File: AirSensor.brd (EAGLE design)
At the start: 108.6 x 80 mm, 32 parts, among them J1 battery Output 7.4V, J2 10118194-0001LF, U1 ATSAMD21G18A-AU, Y1 32.768kHz

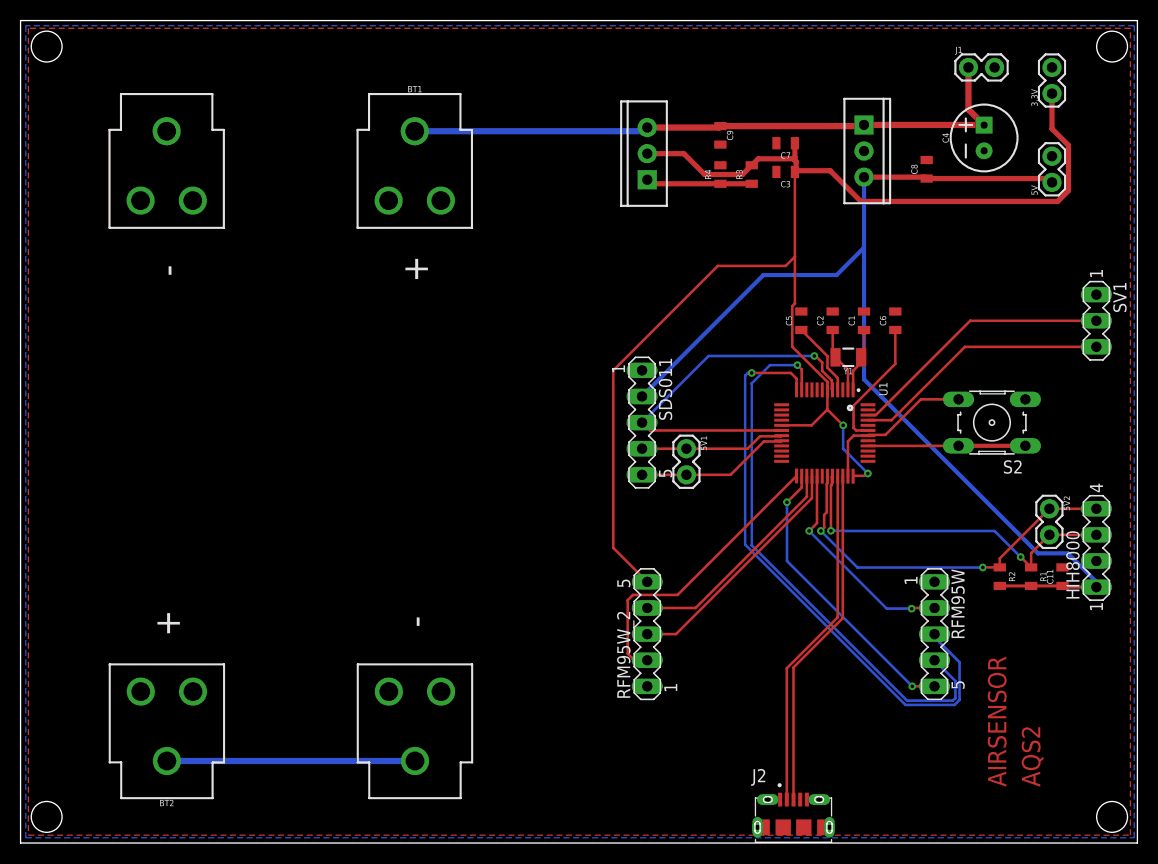
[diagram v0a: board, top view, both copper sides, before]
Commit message: added JTAG schematic and PCB  + all pictures
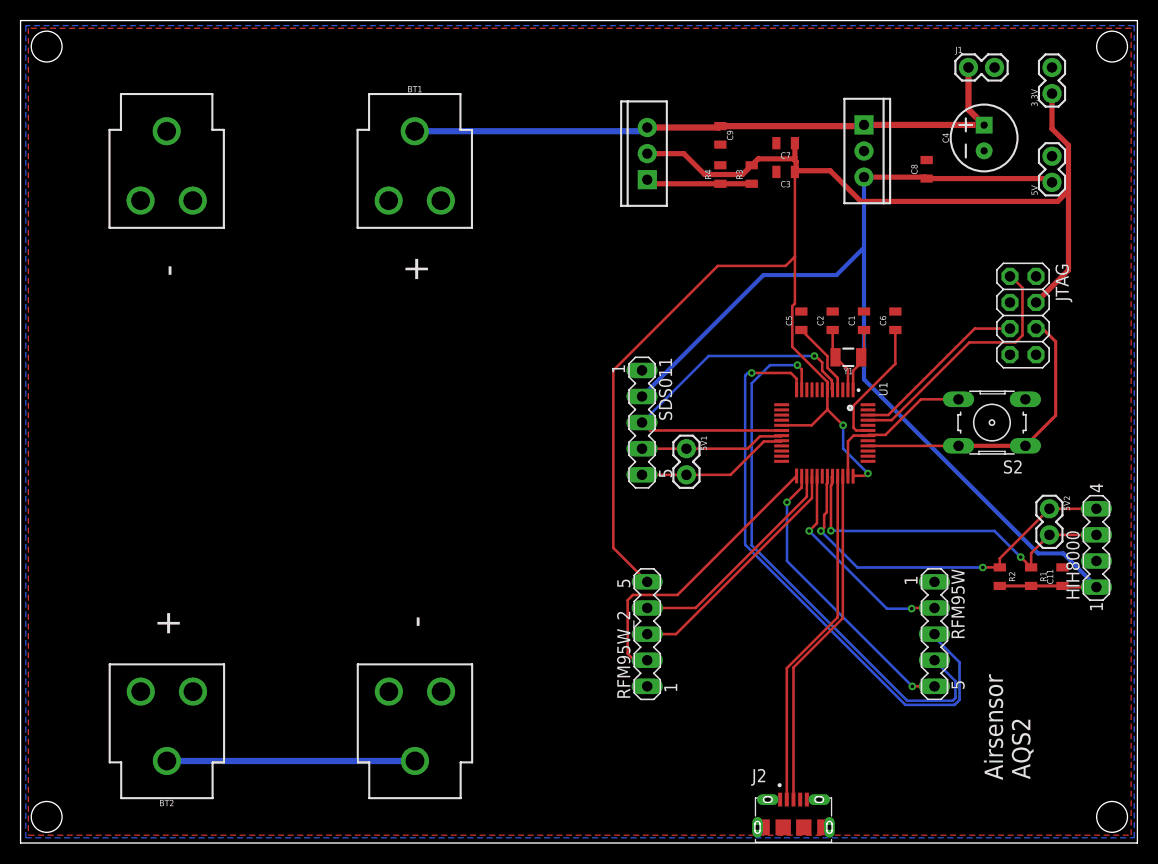
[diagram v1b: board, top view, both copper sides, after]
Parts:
- removed SV1: (no value), con-lstb:MA03-1
- added JTAG: (no value), adafruit:2X04
- HIH8000: value Temp and humid sensor -> T and H sensor
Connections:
- net 3.3V: now also JTAG.4
- net GND: now also JTAG.2
- net N$10: now also JTAG.6
- net N$15: now also JTAG.1; no longer SV1.3
- net N$16: now also JTAG.5; no longer SV1.2
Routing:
- net N$10: track 15.3 -> 29.1 mm
- net 3.3V: track 140.3 -> 152.5 mm
- net N$16: track 26.0 -> 17.3 mm
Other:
- board text added: "Airsensor"
- board text removed: "AIRSENSOR"
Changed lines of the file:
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@@
 <setting verticaltext="up"/>
 </settings>
-<grid distance="5" unitdist="mil" unit="mil" style="dots" multiple="1" display="yes" altdistance="5" altunitdist="mil" altunit="mil"/>
+<grid distance="1" unitdist="mil" unit="mil" style="dots" multiple="1" display="yes" altdistance="5" altunitdist="mil" altunit="mil"/>
 <layers>
 <layer number="1" name="Top" color="4" fill="1" visible="yes" active="yes"/>
@@
 </layers>
 <board>
+<fusionsync huburn="a.YnVzaW5lc3M6c2t5bmV0MTMz" projecturn="a.YnVzaW5lc3M6c2t5bmV0MTMzI0QyMDE5MTAzMTIzMzQxNDY3Ng" f3durn="urn:adsk.wipprod:dm.lineage:1Ub-EbivQau2BrcJynC3oQ" pcbguid="" lastpulledtime="" lastsyncedchangeguid="" latestrevisionid="78f90f56-6bf9-44d5-9f1f-b04a8c04fa7a" lastsyncedrevisionid="78f90f56-6bf9-44d5-9f1f-b04a8c04fa7a" lastboardhashguid="26696e0e-a0db-138f-774c-2213d21c3754" lastpushedtime="2020-10-21T16:27:33Z" linktopcb3d="true"/>
 <plain>
 <wire x1="0" y1="0" x2="108.636" y2="0" width="0" layer="20"/>
@@
 <wire x1="108.636" y1="80" x2="0" y2="80" width="0" layer="20"/>
 <wire x1="0" y1="80" x2="0" y2="0" width="0" layer="20"/>
-<dimension x1="60.96" y1="25.4" x2="88.9" y2="25.4" x3="74.93" y3="28.448" textsize="1.778" layer="1"/>
-<dimension x1="60.96" y1="0.254" x2="60.96" y2="25.4" x3="52.324" y3="12.827" textsize="1.778" layer="1"/>
 <hole x="2.54" y="2.54" drill="3"/>
 <hole x="2.54" y="77.47" drill="3"/>
 <hole x="106.172" y="77.47" drill="3"/>
 <hole x="106.172" y="2.54" drill="3"/>
-<text x="95.885" y="5.461" size="1.778" layer="1" rot="R90">AIRSENSOR</text>
-<text x="99.187" y="5.461" size="1.778" layer="1" rot="R90">AQS2</text>
+<dimension x1="0" y1="0" x2="108.636" y2="0" x3="54.318" y3="-3.7084" textsize="1.778" layer="1"/>
+<dimension x1="0" y1="0" x2="0" y2="80" x3="-2.1336" y3="40" textsize="1.778" layer="1"/>
+<text x="95.5548" y="6.1214" size="1.778" layer="25" rot="R90">Airsensor</text>
+<text x="98.2218" y="6.1976" size="1.778" layer="25" rot="R90">AQS2</text>
 </plain>
 <attributes>
@@
 <attribute name="VALUE" x="57.531" y="43.434" size="1.27" layer="27" ratio="10" rot="R270"/>
 </element>
-<element name="HIH8000" library="con-lstb" library_urn="urn:adsk.eagle:library:162" package="MA04-1" package3d_urn="urn:adsk.eagle:package:8337/1" value="Temp and humid sensor" x="104.648" y="28.702" smashed="yes" rot="R90">
+<element name="HIH8000" library="con-lstb" library_urn="urn:adsk.eagle:library:162" package="MA04-1" package3d_urn="urn:adsk.eagle:package:8337/1" value="T and H sensor" x="104.648" y="28.702" smashed="yes" rot="R90">
 <attribute name="MF" value="" x="104.648" y="28.702" size="1.778" layer="27" rot="R90" display="off"/>
 <attribute name="MPN" value="" x="104.648" y="28.702" size="1.778" layer="27" rot="R90" display="off"/>
@@
 <attribute name="OC_NEWARK" value="unknown" x="104.648" y="28.702" size="1.778" layer="27" rot="R90" display="off"/>
 <attribute name="POPULARITY" value="41" x="104.648" y="28.702" size="1.778" layer="27" rot="R90" display="off"/>
-<attribute name="VALUE" x="102.997" y="29.337" size="1.27" layer="27" ratio="10" rot="R90"/>
-</element>
-<element name="SV1" library="con-lstb" library_urn="urn:adsk.eagle:library:162" package="MA03-1" package3d_urn="urn:adsk.eagle:package:8339/1" value="" x="104.648" y="50.8" smashed="yes" rot="R270">
-<attribute name="MF" value="" x="104.648" y="50.8" size="1.778" layer="27" rot="R270" display="off"/>
-<attribute name="MPN" value="" x="104.648" y="50.8" size="1.778" layer="27" rot="R270" display="off"/>
-<attribute name="NAME" x="106.299" y="54.61" size="1.27" layer="25" ratio="10" rot="R270"/>
-<attribute name="OC_FARNELL" value="unknown" x="104.648" y="50.8" size="1.778" layer="27" rot="R270" display="off"/>
-<attribute name="OC_NEWARK" value="unknown" x="104.648" y="50.8" size="1.778" layer="27" rot="R270" display="off"/>
-<attribute name="POPULARITY" value="48" x="104.648" y="50.8" size="1.778" layer="27" rot="R270" display="off"/>
-<attribute name="VALUE" x="101.727" y="54.61" size="1.27" layer="27" ratio="10" rot="R270"/>
+<attribute name="VALUE" x="107.5182" y="22.5806" size="1.27" layer="27" ratio="10" rot="R90"/>
 </element>
 <element name="RFM95W" library="con-lstb" library_urn="urn:adsk.eagle:library:162" package="MA05-1" package3d_urn="urn:adsk.eagle:package:8332/1" value="LoRa1" x="88.9" y="20.32" smashed="yes" rot="R270">
@@
 <attribute name="PROD_ID" value="CAP-08064" x="101.346" y="25.908" size="1.778" layer="27" rot="R90" display="off"/>
 <attribute name="VALUE" x="102.235" y="25.908" size="0.6096" layer="27" font="vector" ratio="20" rot="R90" align="top-center"/>
+</element>
+<element name="JTAG" library="adafruit" library_urn="urn:adsk.eagle:library:420" package="2X04" package3d_urn="urn:adsk.eagle:package:6240893/1" value="" x="97.5106" y="51.308" smashed="yes" rot="R270">
+<attribute name="NAME" x="100.6856" y="56.388" size="1.27" layer="25" ratio="10" rot="R270"/>
+<attribute name="VALUE" x="93.0656" y="56.388" size="1.27" layer="27" rot="R270"/>
 </element>
 </elements>
@@
 <vertex x="0.762" y="79.248"/>
 <vertex x="0.762" y="0.762"/>
-<vertex x="107.95" y="0.762"/>
-<vertex x="107.95" y="79.248"/>
+<vertex x="108.0262" y="0.762"/>
+<vertex x="108.0262" y="79.248"/>
 </polygon>
 <polygon width="0.1524" layer="16" isolate="0.508">
@@
 <wire x1="81.03" y1="39.628" x2="82.432" y2="39.628" width="0.254" layer="1"/>
 <wire x1="80.482" y1="39.08" x2="81.03" y2="39.628" width="0.254" layer="1"/>
+<contactref element="JTAG" pad="2"/>
 <wire x1="73.522" y1="68.072" x2="73.522" y2="65.278" width="0" layer="19" extent="1-1"/>
 </signal>
@@
 <wire x1="91.2368" y1="38.6334" x2="87.8278" y2="38.628" width="0.254" layer="1"/>
 <wire x1="87.8278" y1="38.628" x2="82.432" y2="38.628" width="0.254" layer="1"/>
+<contactref element="JTAG" pad="6"/>
+<wire x1="97.7392" y1="38.6334" x2="100.6856" y2="41.5798" width="0.3048" layer="1"/>
+<wire x1="100.6856" y1="41.5798" x2="100.6856" y2="48.768" width="0.3048" layer="1"/>
+<wire x1="100.6856" y1="48.768" x2="99.4156" y2="50.038" width="0.3048" layer="1"/>
+<wire x1="99.4156" y1="50.038" x2="98.7806" y2="50.038" width="0.3048" layer="1"/>
 </signal>
 <signal name="N$11">
@@
 <wire x1="79.375" y1="55.245" x2="82.042" y2="57.912" width="0.4064" layer="16"/>
 <wire x1="82.042" y1="57.912" x2="82.042" y2="64.77" width="0.4064" layer="16"/>
-<wire x1="104.648" y1="24.892" x2="104.648" y2="25.4" width="0.4064" layer="16"/>
-<wire x1="104.648" y1="25.4" x2="101.8794" y2="28.1686" width="0.4064" layer="16"/>
-<wire x1="101.8794" y1="28.1686" x2="98.97806875" y2="28.1686" width="0.4064" layer="16"/>
+<wire x1="104.648" y1="24.892" x2="104.648" y2="24.9428" width="0.4064" layer="16"/>
+<wire x1="104.648" y1="24.9428" x2="101.4222" y2="28.1686" width="0.4064" layer="16"/>
+<wire x1="101.4222" y1="28.1686" x2="98.97806875" y2="28.1686" width="0.4064" layer="16"/>
 <wire x1="98.97806875" y1="28.1686" x2="82.042" y2="45.10466875" width="0.4064" layer="16"/>
 <wire x1="82.042" y1="45.10466875" x2="82.042" y2="57.912" width="0.4064" layer="16"/>
@@
 <wire x1="82.423" y1="35.941" x2="82.204" y2="35.722" width="0.254" layer="1"/>
 <wire x1="82.204" y1="35.722" x2="81.026" y2="35.722" width="0.254" layer="1"/>
+<contactref element="JTAG" pad="4"/>
+<wire x1="98.7806" y1="52.578" x2="101.9302" y2="55.7276" width="0.508" layer="1"/>
+<wire x1="101.9302" y1="55.7276" x2="101.9302" y2="63.45038125" width="0.508" layer="1"/>
 <wire x1="80.01" y1="40.628" x2="82.432" y2="40.628" width="0" layer="19" extent="1-1"/>
 </signal>
@@
 </signal>
 <signal name="N$15">
-<contactref element="SV1" pad="3"/>
 <contactref element="U1" pad="45"/>
-<wire x1="104.648" y1="48.26" x2="91.85813125" y2="48.26" width="0.254" layer="1"/>
-<wire x1="84.72613125" y1="41.128" x2="82.432" y2="41.128" width="0.254" layer="1"/>
-<wire x1="91.85813125" y1="48.26" x2="84.72613125" y2="41.128" width="0.254" layer="1"/>
+<wire x1="82.432" y1="41.128" x2="84.72613125" y2="41.128" width="0.254" layer="1"/>
+<contactref element="JTAG" pad="1"/>
+<wire x1="92.28993125" y1="48.6918" x2="96.774" y2="48.6918" width="0.254" layer="1"/>
+<wire x1="96.774" y1="48.6918" x2="97.4598" y2="49.3776" width="0.254" layer="1"/>
+<wire x1="97.4598" y1="49.3776" x2="97.4598" y2="54.0004" width="0.254" layer="1"/>
+<wire x1="97.4598" y1="54.0004" x2="96.3422" y2="55.118" width="0.254" layer="1"/>
+<wire x1="96.3422" y1="55.118" x2="96.2406" y2="55.118" width="0.254" layer="1"/>
+<wire x1="84.72613125" y1="41.128" x2="92.28993125" y2="48.6918" width="0.254" layer="1"/>
 </signal>
 <signal name="N$16">
 <contactref element="U1" pad="46"/>
-<contactref element="SV1" pad="2"/>
-<wire x1="104.648" y1="50.8" x2="92.37413125" y2="50.8" width="0.254" layer="1"/>
-<wire x1="83.20213125" y1="41.628" x2="82.432" y2="41.628" width="0.254" layer="1"/>
-<wire x1="92.37413125" y1="50.8" x2="83.20213125" y2="41.628" width="0.254" layer="1"/>
+<contactref element="JTAG" pad="5"/>
+<wire x1="92.8116" y1="50.038" x2="96.2406" y2="50.038" width="0.254" layer="1"/>
+<wire x1="82.432" y1="41.628" x2="84.4016" y2="41.628" width="0.254" layer="1"/>
+<wire x1="84.4016" y1="41.628" x2="92.8116" y2="50.038" width="0.254" layer="1"/>
 </signal>
 <signal name="SS">
@@
 </note>
 <note version="8.3" severity="warning">
+Since Version 8.3, EAGLE supports Fusion synchronisation.
+This feature will not be available in this version and saving
+the document will break the link to the Fusion PCB feature.
+</note>
+<note version="8.3" severity="warning">
